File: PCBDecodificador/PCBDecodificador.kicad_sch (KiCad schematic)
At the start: 2 parts, among them J1 Conector Mic 8 Vias, J2 Conector Mic 8 Vias

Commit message: Adicionado PDF do Cabo Amplificador Decodificador
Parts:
- removed J2: Conector Mic 8 Vias, symbol Connector:Conn_01x08_Pin
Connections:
- net 13 - 20 MHz: no longer names the net of J1.5 (Pin_5)
- net 2 - 3 MHz: no longer names the net of J1.1 (Pin_1)
- net 20 - 30 MHz: no longer names the net of J1.6 (Pin_6)
- net 3 - 5 MHz: no longer names the net of J1.2 (Pin_2)
- net 5 - 8 MHz: no longer names the net of J1.3 (Pin_3)
- net 8 - 13 MHz: no longer names the net of J1.4 (Pin_4)
- net GND: no longer names the net of J1.8 (Pin_8)
- net PTT: no longer names the net of J1.7 (Pin_7)
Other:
- note removed: "3m"
- title: Cabo Amplificador Decodificador -> PCB Decodificador

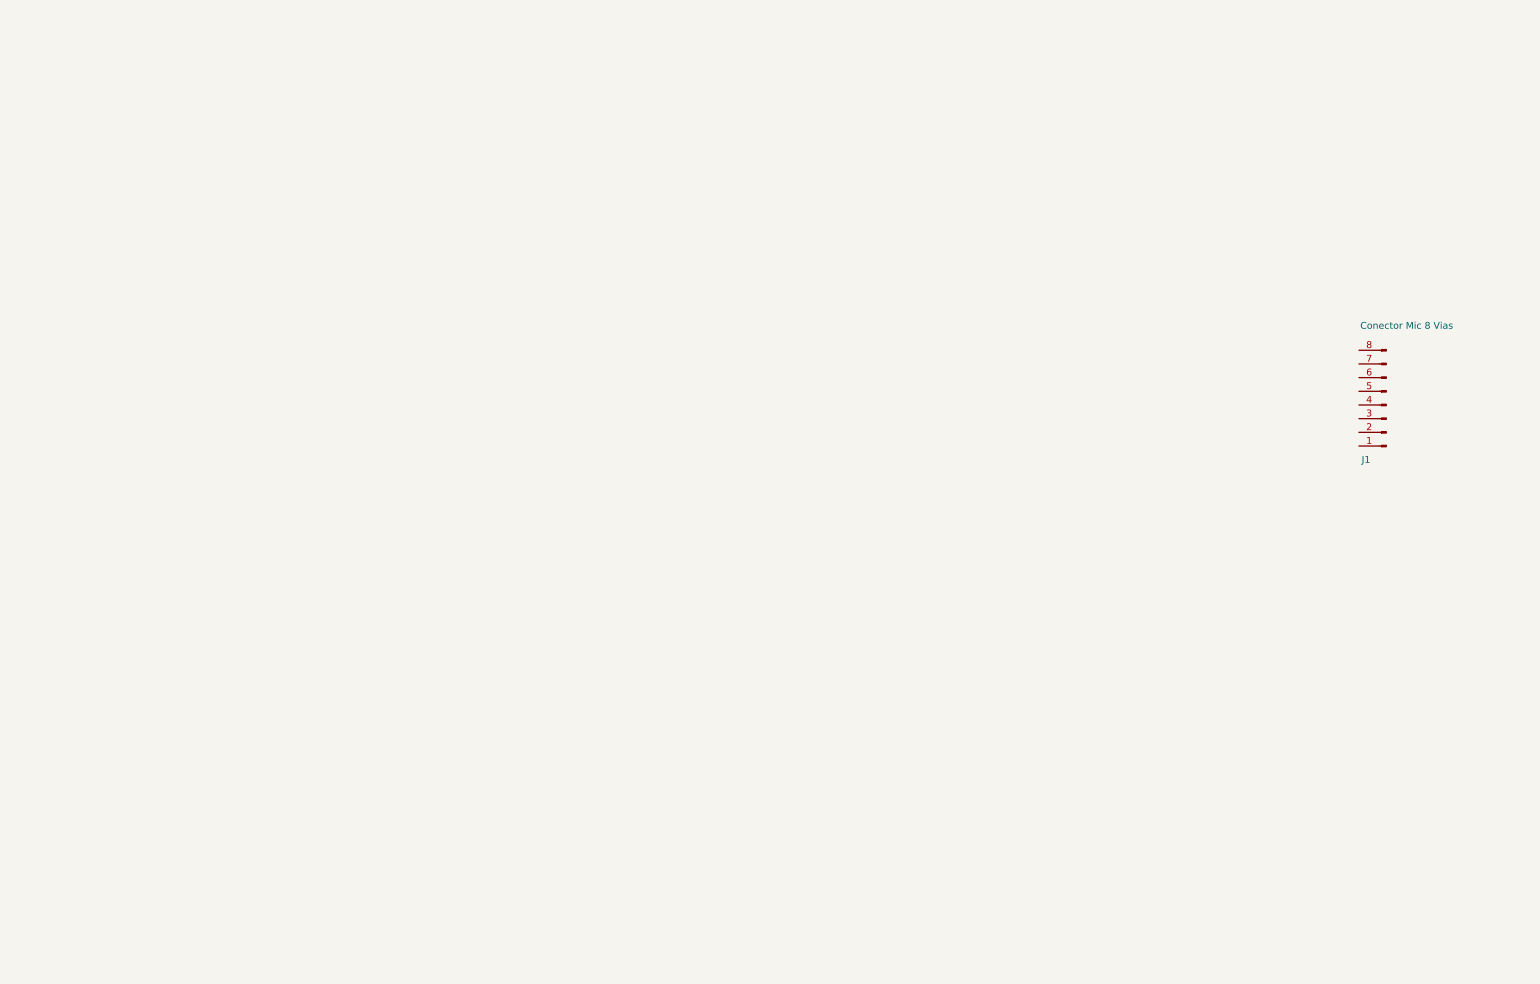
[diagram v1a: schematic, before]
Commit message: PCB do decodificador, ainda falta verificar parte do PTT e se vamos manter a banda de 2 - 3MHz no conector
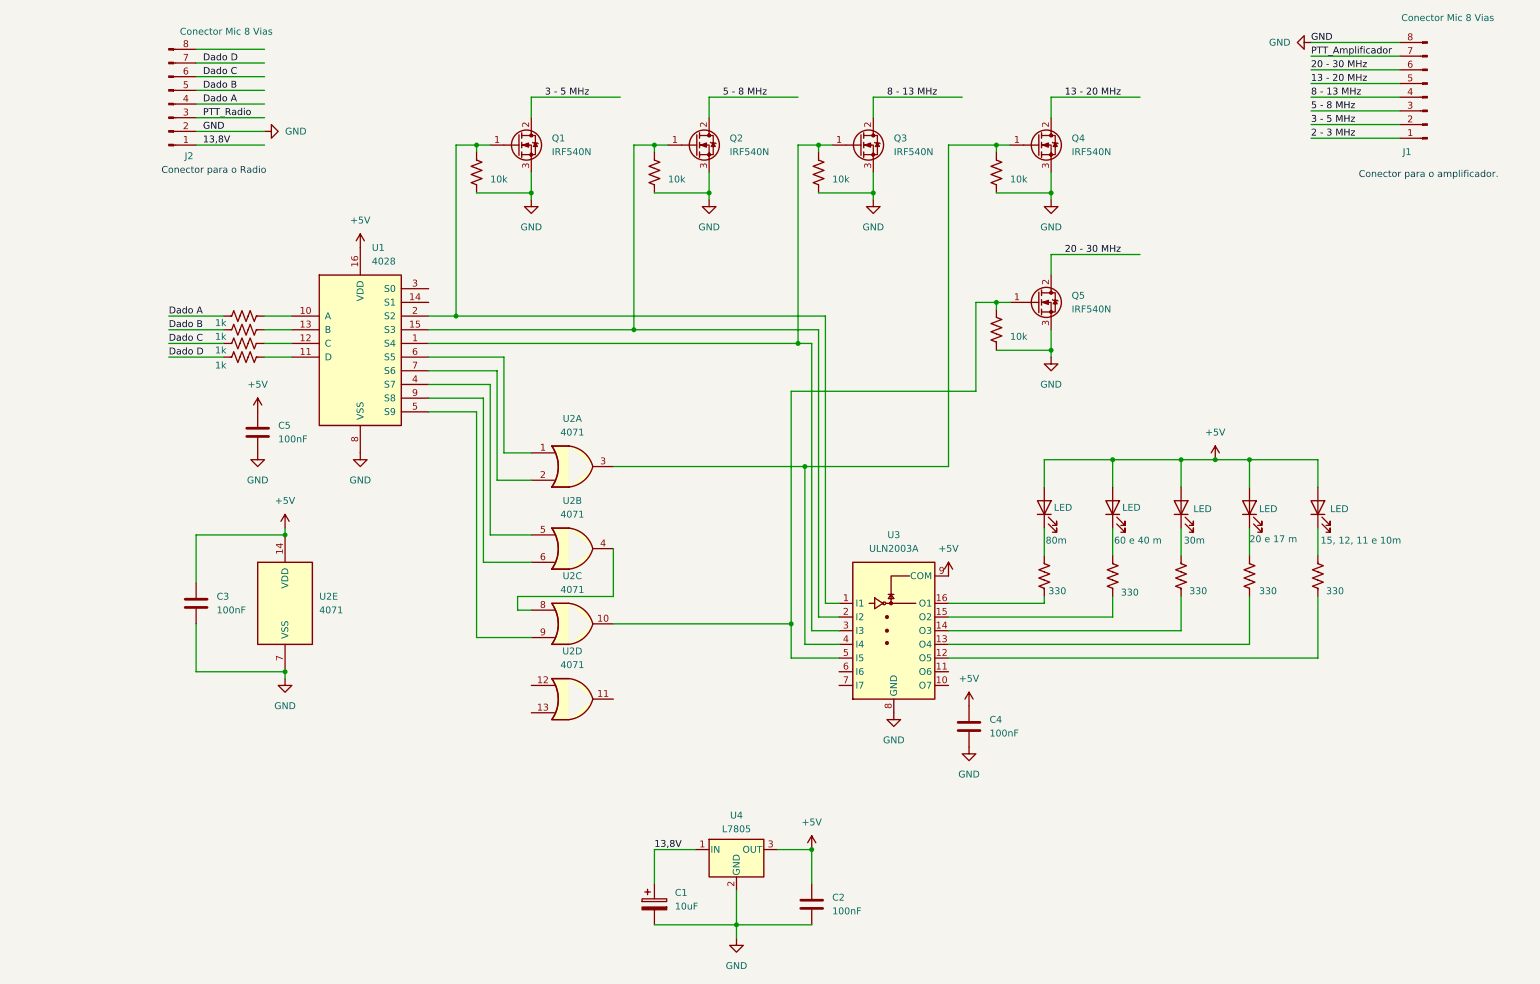
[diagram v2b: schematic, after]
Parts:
- added C1: 10uF, symbol Device:C_Polarized
- added C2, C3, C4, C5: 100nF, symbol Device:C
- added D1, D2, D3, D4, D5: LED, symbol Device:LED
- added J2: Conector Mic 8 Vias, symbol Connector:Conn_01x08_Pin
- added Q1, Q2, Q3, Q4, Q5: IRF540N, Package_TO_SOT_THT:TO-220-3_Vertical, symbol Transistor_FET:IRF540N
- added R1, R2, R3, R4: 1k, symbol Device:R_US
- added R10, R11, R12, R13, R14: 10k, symbol Device:R_US
- added R5, R6, R7, R8, R9: 330, symbol Device:R_US
- added U1: 4028, symbol 4xxx:4028
- added U2: 4071, symbol 4xxx:4071
- added U3: ULN2003A, symbol Transistor_Array:ULN2003A
- added U4: L7805, symbol Regulator_Linear:L7805
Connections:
- net 2 - 3 MHz: now reaches J1.1 (Pin_1)
- net 3 - 5 MHz: now reaches J1.2 (Pin_2)
- net 3 - 5 MHz: now also Q1.2 (D)
- net 5 - 8 MHz: now reaches J1.3 (Pin_3)
- net 5 - 8 MHz: now also Q2.2 (D)
- net 8 - 13 MHz: now reaches J1.4 (Pin_4)
- net 8 - 13 MHz: now also Q3.2 (D)
- net 13 - 20 MHz: now reaches J1.5 (Pin_5)
- net 13 - 20 MHz: now also Q4.2 (D)
- net 20 - 30 MHz: now reaches J1.6 (Pin_6)
- net 20 - 30 MHz: now also Q5.2 (D)
- net PTT_Amplificador: now reaches J1.7 (Pin_7)
- net GND: now reaches J1.8 (Pin_8)
- net GND: now also C1.2, C2.2, C3.2, C4.2, C5.2, J2.2 (Pin_2), Q1.3 (S), Q2.3 (S), Q3.3 (S), Q4.3 (S), Q5.3 (S), R10.2, R11.2, R12.2, R13.2, R14.2, U1.8 (VSS), U2.7 (VSS), U3.8 (GND), U4.2 (GND)
- new net: Q1.1 (G), R10.1, U1.2 (S2), U3.1 (I1)
- new net: D2.1 (K), R6.1
- new net: R6.2, U3.15 (O2)
- new net: Q3.1 (G), R12.1, U1.1 (S4), U3.3 (I3)
- new net: R9.2, U3.12 (O5)
- new net: R8.2, U3.13 (O4)
- new net: R7.2, U3.14 (O3)
- new net: R5.2, U3.16 (O1)
- new net: Q2.1 (G), R11.1, U1.15 (S3), U3.2 (I2)
- new net: Q4.1 (G), R13.1, U2.3, U3.4 (I4)
- new net: Q5.1 (G), R14.1, U2.10, U3.5 (I5)
- new net: D4.1 (K), R8.1
- new net: D5.1 (K), R9.1
- new net: U2.4, U2.8
- new net: U1.4 (S7), U2.5
- new net: U1.9 (S8), U2.6
- new net: D3.1 (K), R7.1
- new net: D1.1 (K), R5.1
- new net: U1.6 (S5), U2.1
- new net: U1.7 (S6), U2.2
- new net: U1.5 (S9), U2.9
- new net: R4.2, U1.11 (D)
- new net: R1.2, U1.10 (A)
- new net: R2.2, U1.13 (B)
- new net: R3.1, U1.12 (C)
- new net +5V: C2.1, C3.1, C4.1, C5.1, D1.2 (A), D2.2 (A), D3.2 (A), D4.2 (A), D5.2 (A), U1.16 (VDD), U2.14 (VDD), U3.9 (COM), U4.3 (OUT)
- new net 13,8V: C1.1, J2.1 (Pin_1), U4.1 (IN)
- new net Dado A: J2.4 (Pin_4), R1.1
- new net Dado B: J2.5 (Pin_5), R2.1
- new net Dado C: J2.6 (Pin_6), R3.2
- new net Dado D: J2.7 (Pin_7), R4.1
- new net PTT_Radio: J2.3 (Pin_3)
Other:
- note added: "Conector para o Radio"
- note added: "Conector para o amplificador."
- moved on the sheet: J1

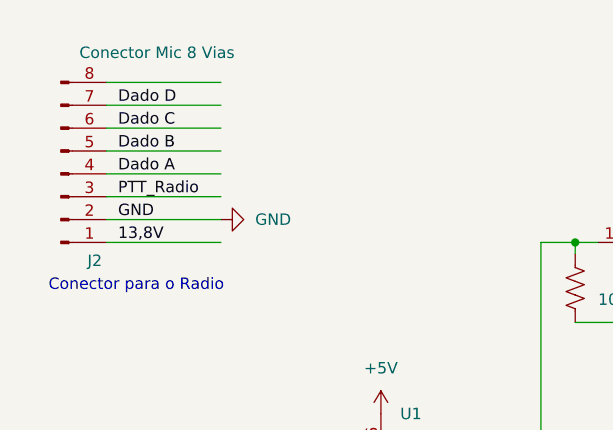
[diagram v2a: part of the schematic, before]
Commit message: Adicionado CaboYaesuDecodificador
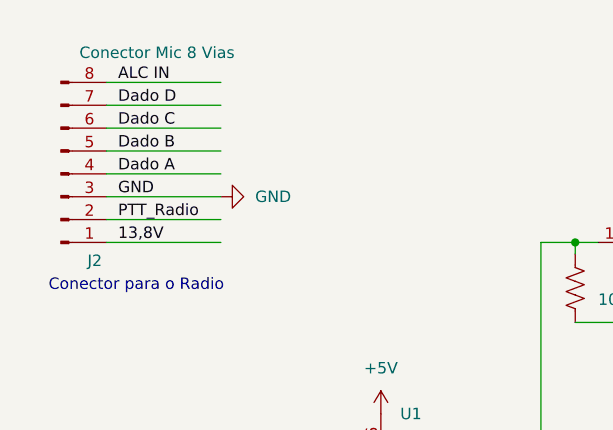
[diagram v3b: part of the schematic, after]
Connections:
- net GND: now also J2.3 (Pin_3); no longer J2.2 (Pin_2)
- net PTT_Radio: now also J2.2 (Pin_2); no longer J2.3 (Pin_3)
- net ALC IN: now reaches J2.8 (Pin_8)
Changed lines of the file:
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@@
 	)
 	(label "GND"
-		(at 39.37 40.64 0)
+		(at 39.37 38.1 0)
 		(effects
 			(font
@@
 		)
 	)
+	(label "ALC IN"
+		(at 39.37 25.4 0)
+		(effects
+			(font
+				(size 1.27 1.27)
+			)
+			(justify left bottom)
+		)
+	)
 	(label "5 - 8 MHz"
 		(at 135.89 34.29 0)
@@
 	)
 	(label "PTT_Radio"
-		(at 39.37 38.1 0)
+		(at 39.37 40.64 0)
 		(effects
 			(font
@@
 	(symbol
 		(lib_id "power:GND")
-		(at 50.8 40.64 90)
+		(at 50.8 38.1 90)
 		(unit 1)
 		(exclude_from_sim no)
@@
 		(fields_autoplaced yes)
 		(property "Reference" "#PWR04"
-			(at 57.15 40.64 0)
+			(at 57.15 38.1 0)
 			(effects
 				(font
@@
 		)
 		(property "Value" "GND"
-			(at 54.61 40.6399 90)
+			(at 54.61 38.0999 90)
 			(effects
 				(font
@@
 		)
 		(property "Footprint" ""
-			(at 50.8 40.64 0)
+			(at 50.8 38.1 0)
 			(effects
 				(font
@@
 		)
 		(property "Datasheet" ""
-			(at 50.8 40.64 0)
+			(at 50.8 38.1 0)
 			(effects
 				(font
@@
 		)
 		(property "Description" "Power symbol creates a global label with name \"GND\" , ground"
-			(at 50.8 40.64 0)
-			(effects
-				(font
+			(at 50.8 38.1 0)
+			(effects
+				(font

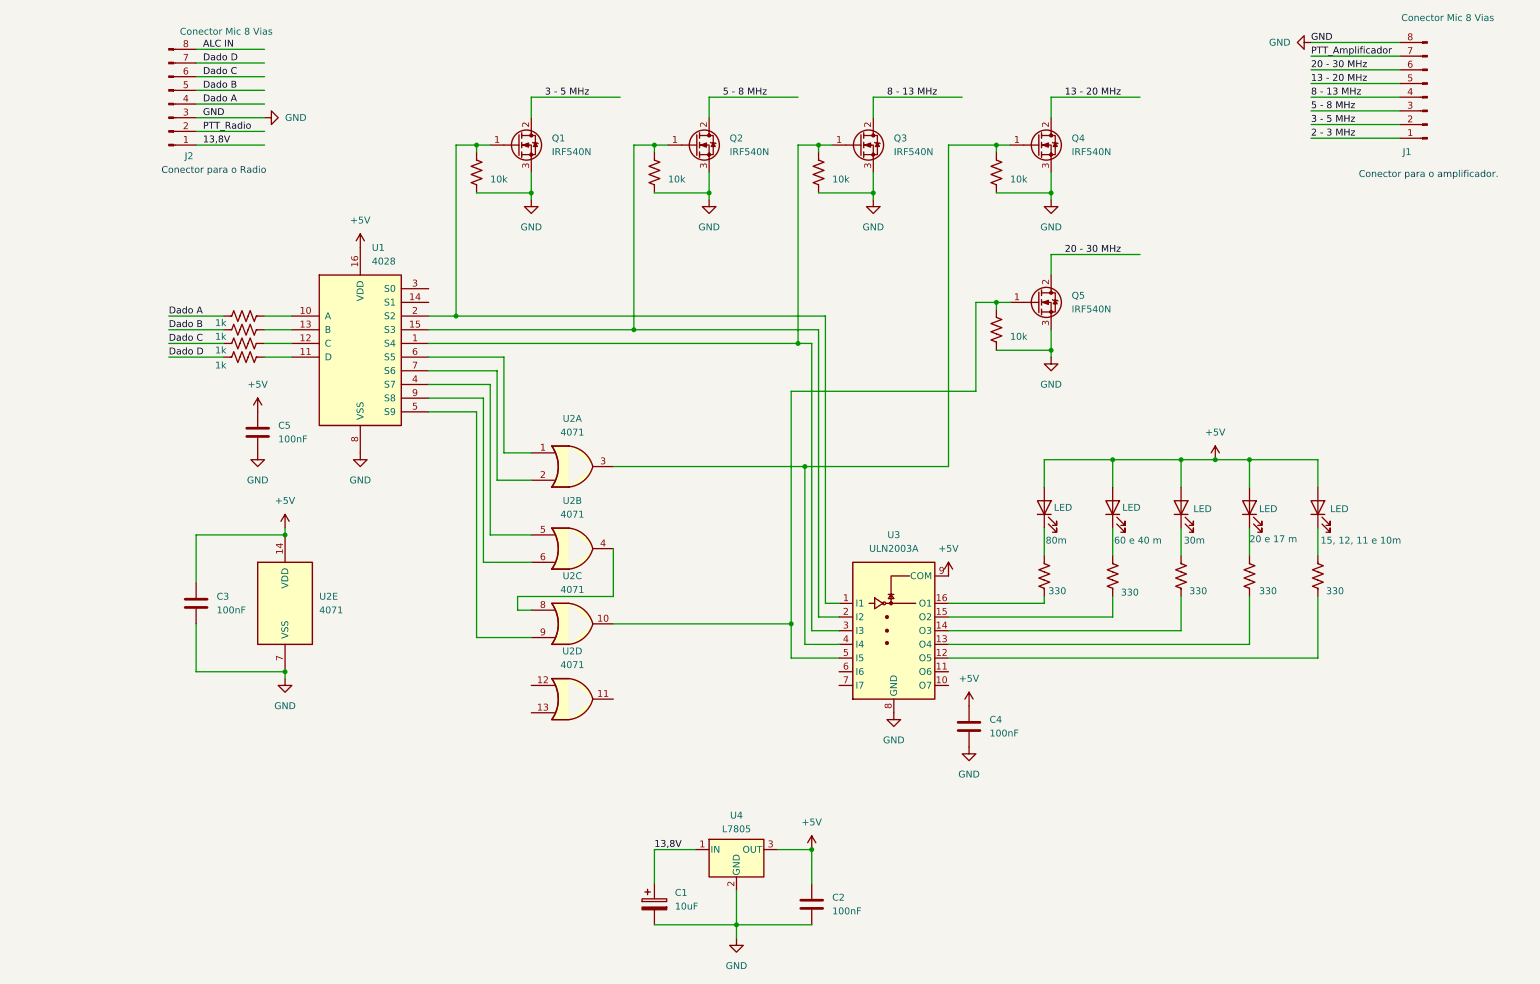
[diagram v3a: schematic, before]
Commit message: Adicionado cabo do PTT Yaesu. Finalizado a placa do decodificador.
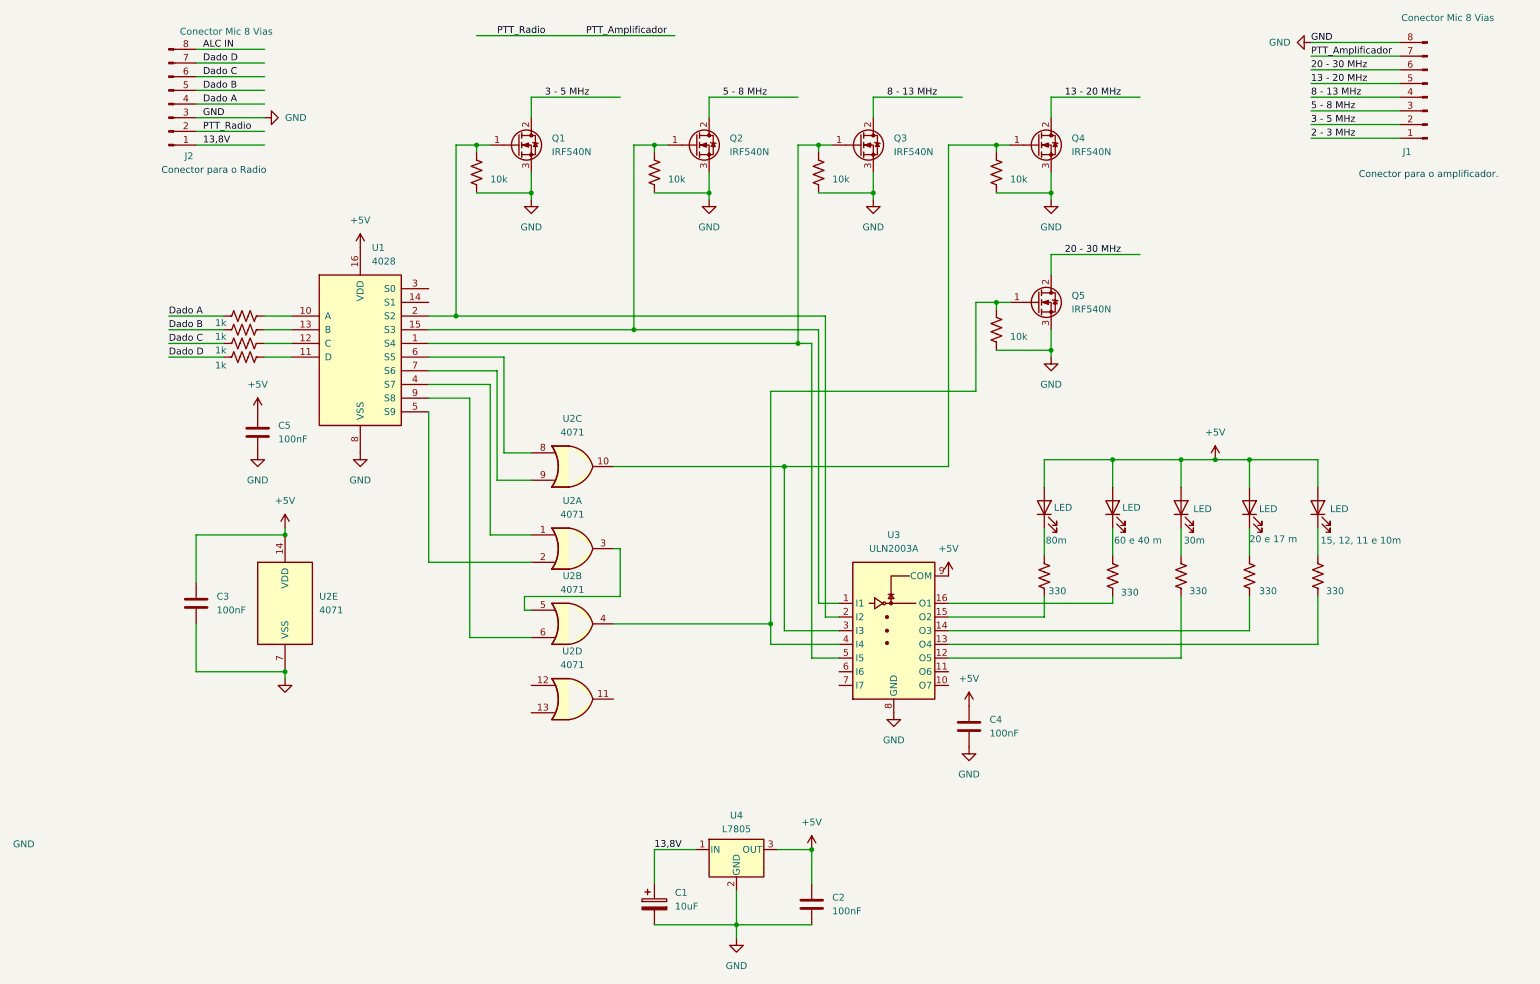
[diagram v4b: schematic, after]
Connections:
- net PTT_Radio is gone; now on net PTT_Amplificador: J2.2 (Pin_2)
- net at Q1.1 (G), R10.1, U1.2 (S2): now also U3.2 (I2); no longer U3.1 (I1)
- net at R6.2: now also U3.16 (O1); no longer U3.15 (O2)
- net at Q3.1 (G), R12.1, U1.1 (S4): now also U3.5 (I5); no longer U3.3 (I3)
- net at U3.12 (O5): now also R7.2; no longer R9.2
- net at U3.13 (O4): now also R9.2; no longer R8.2
- net at U3.14 (O3): now also R8.2; no longer R7.2
- net at R5.2: now also U3.15 (O2); no longer U3.16 (O1)
- net at Q2.1 (G), R11.1, U1.15 (S3): now also U3.1 (I1); no longer U3.2 (I2)
- net at Q4.1 (G), R13.1: now also U2.10, U3.3 (I3); no longer U2.3, U3.4 (I4)
- net at Q5.1 (G), R14.1: now also U2.4, U3.4 (I4); no longer U2.10, U3.5 (I5)
- net at U2.8: now also U1.6 (S5); no longer U2.4
- net at U2.5: now also U2.3; no longer U1.4 (S7)
- net at U2.1: now also U1.4 (S7); no longer U1.6 (S5)
- net at U2.2: now also U1.5 (S9); no longer U1.7 (S6)
- net at U2.9: now also U1.7 (S6); no longer U1.5 (S9)
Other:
- moved on the sheet: U2A, U2B, U2C
